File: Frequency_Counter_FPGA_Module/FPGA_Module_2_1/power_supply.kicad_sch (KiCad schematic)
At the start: 51 parts, among them U23 LMR33630ADDAR, U24 LMR33630ADDAR, U25 B0505S-1W

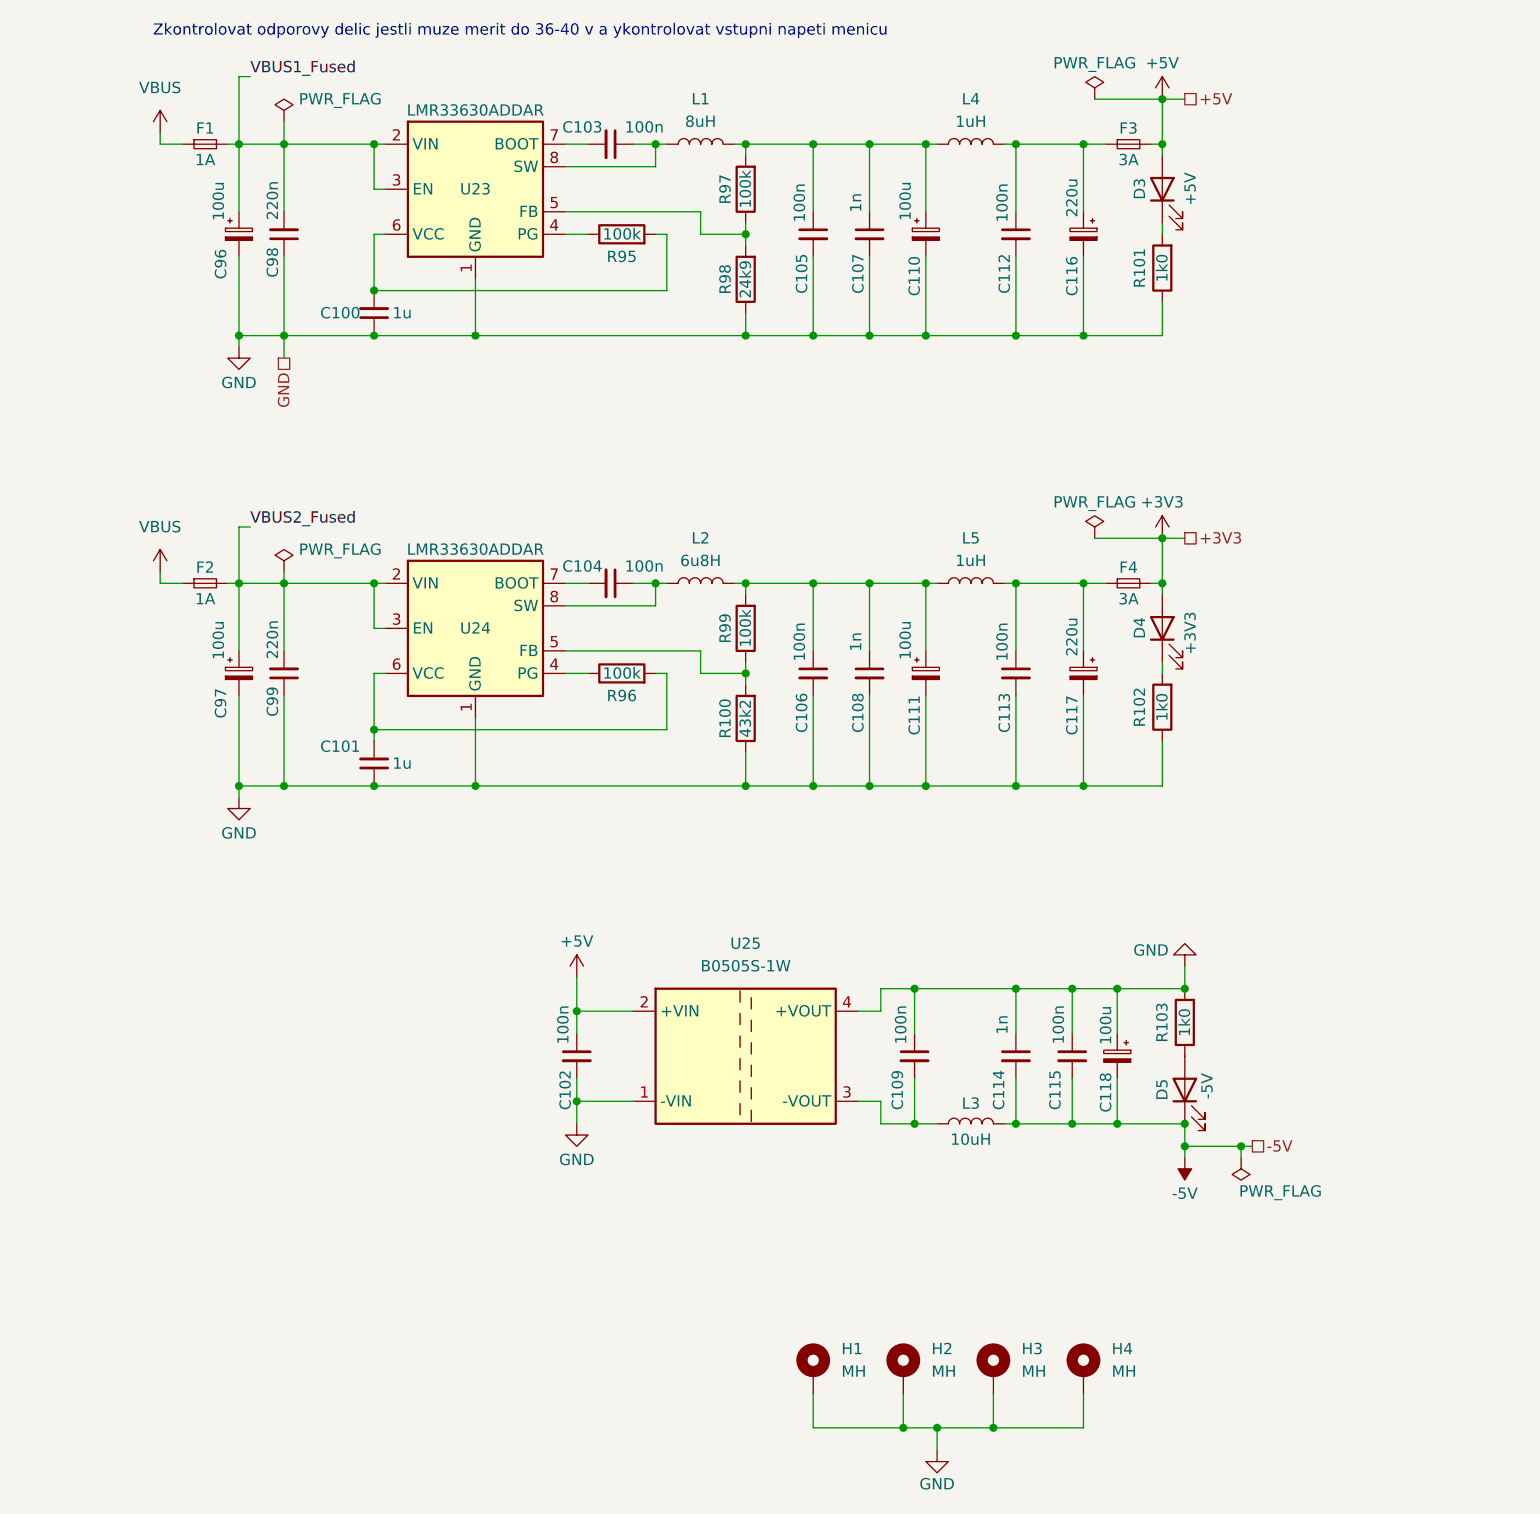
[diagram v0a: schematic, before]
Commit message: chore(hw): KiCad nosne desky FPGA 2.0 -> 2.1 (vc. Gerberu)
Zalohy KiCadu (FPGA_module-backups/, *-bak) ignoruje .gitignore.

Co-Authored-By: Claude Opus 5.5 <noreply@anthropic.com>
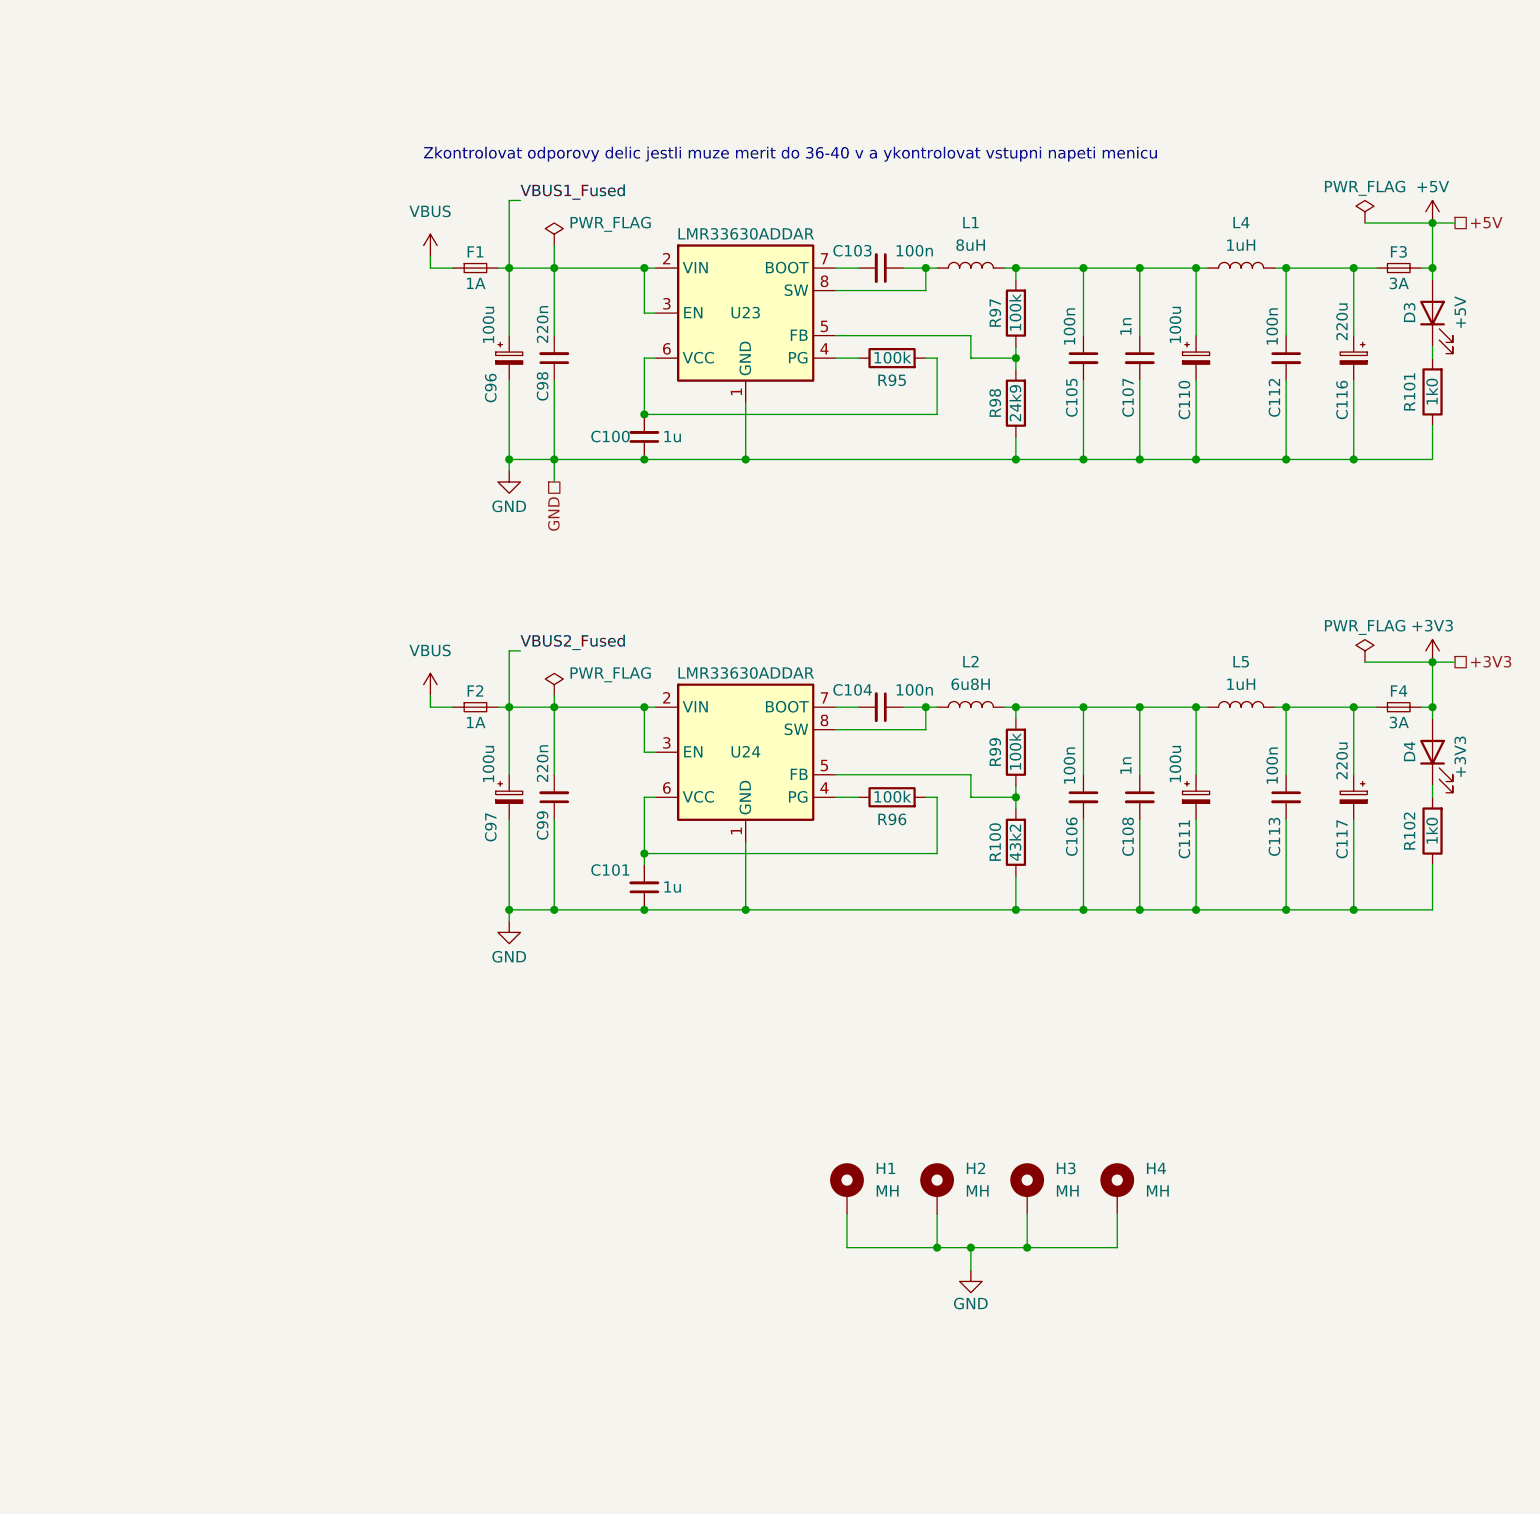
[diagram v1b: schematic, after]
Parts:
- removed C102, C109, C115: 100n, Capacitor_SMD:C_0805_2012Metric, symbol Device:C_Small
- removed C114: 1n, Capacitor_SMD:C_0805_2012Metric, symbol Device:C_Small
- removed C118: 100u, Capacitor_SMD:CP_Elec_6.3x5.4, symbol Device:C_Polarized_Small
- removed D5: -5V, LED_SMD:LED_0805_2012Metric, symbol Device:LED
- removed L3: 10uH, Resistor_SMD:R_0805_2012Metric, symbol Device:L
- removed R103: 1k0, Resistor_SMD:R_0805_2012Metric, symbol Device:R
- removed U25: B0505S-1W, Converter_DCDC:Converter_DCDC_Murata_CRE1xxxxxxSC_THT, symbol Regulator_Switching:CRE1S0505SC
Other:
- moved on the sheet: C100, C101, C103, C104, C105, C106, C107, C108, C110, C111, C112, C113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
